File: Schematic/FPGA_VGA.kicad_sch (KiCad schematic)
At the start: 5 parts, among them U101 Upduino_3.0, Y101 25.175 MHz 7050 3.3V

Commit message: change host bus signal names to match logic
This was a bit of a tedious change, but I think it's
worthwhile to make it more obvious how the logic
and schematic relate to each other.
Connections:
- net HostA0 renamed HostBusAddr0
- net HostA1 renamed HostBusAddr1
- net HostA10 renamed HostBusAddr10
- net HostA2 renamed HostBusAddr2
- net HostA3 renamed HostBusAddr3
- net HostA4 renamed HostBusAddr4
- net HostA5 renamed HostBusAddr5
- net HostA6 renamed HostBusAddr6
- net HostA7 renamed HostBusAddr7
- net HostA8 renamed HostBusAddr8
- net HostA9 renamed HostBusAddr9
- net HostD0 renamed HostBusData0
- net HostD1 renamed HostBusData1
- net HostD2 renamed HostBusData2
- net HostD3 renamed HostBusData3
- net HostD4 renamed HostBusData4
- net HostD5 renamed HostBusData5
- net HostD6 renamed HostBusData6
- net HostD7 renamed HostBusData7
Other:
- sheet HostInterface ports: added HostBusAddr0, HostBusAddr1, HostBusAddr10, HostBusAddr2, HostBusAddr3, HostBusAddr4, HostBusAddr5, HostBusAddr6, HostBusAddr7, HostBusAddr8, HostBusAddr9, HostBusData0, HostBusData1, HostBusData2, HostBusData3, HostBusData4, HostBusData5, HostBusData6, HostBusData7; removed HostA0, HostA1, HostA10, HostA2, HostA3, HostA4, HostA5, HostA6, HostA7, HostA8, HostA9, HostD0, HostD1, HostD2, HostD3, HostD4, HostD5, HostD6, HostD7

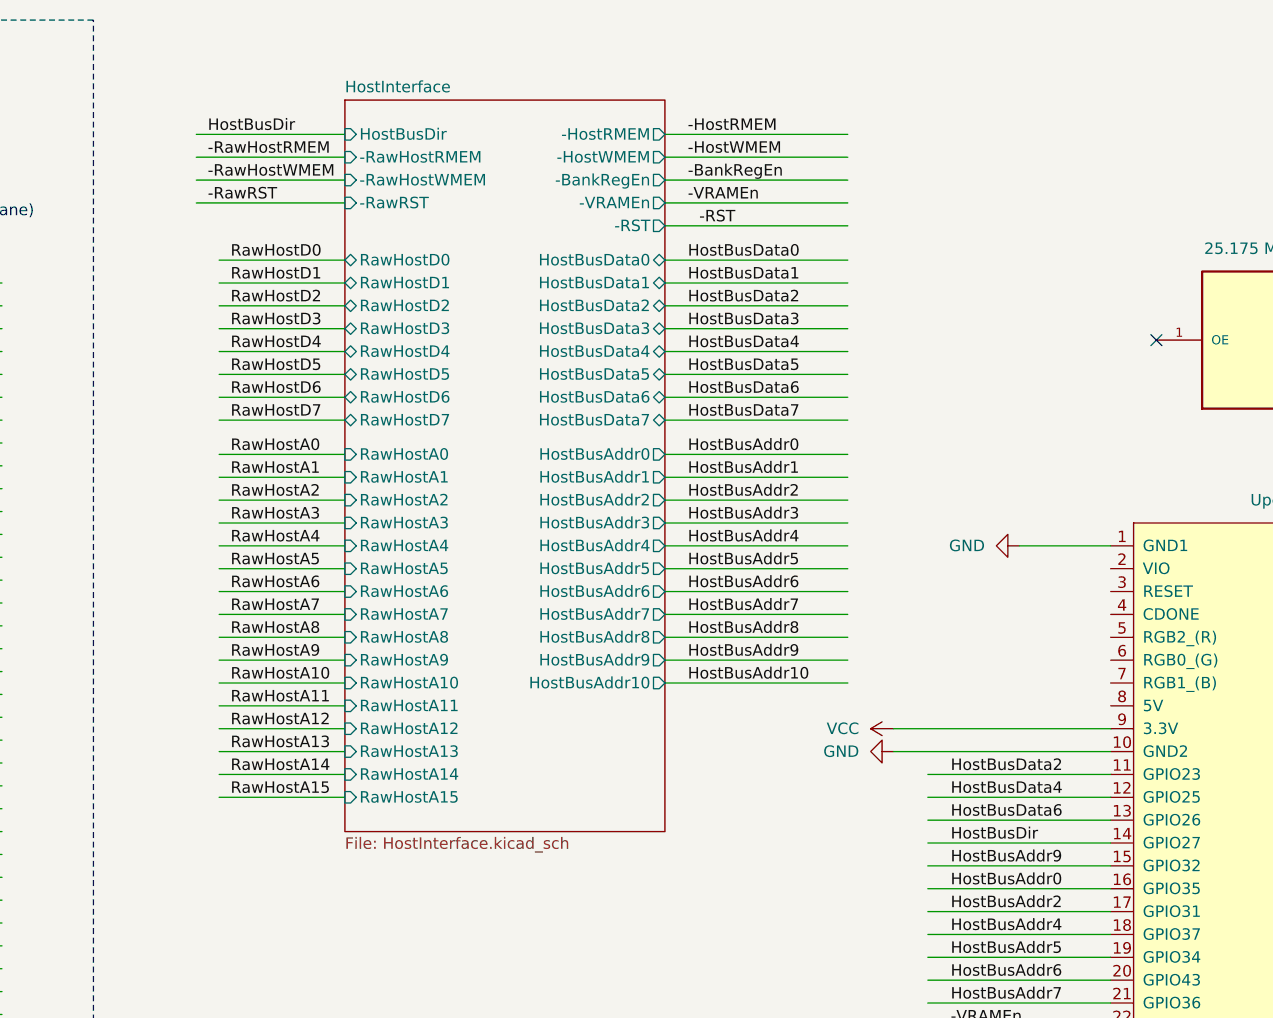
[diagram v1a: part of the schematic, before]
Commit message: connect FPGA 5V pin to host +5V
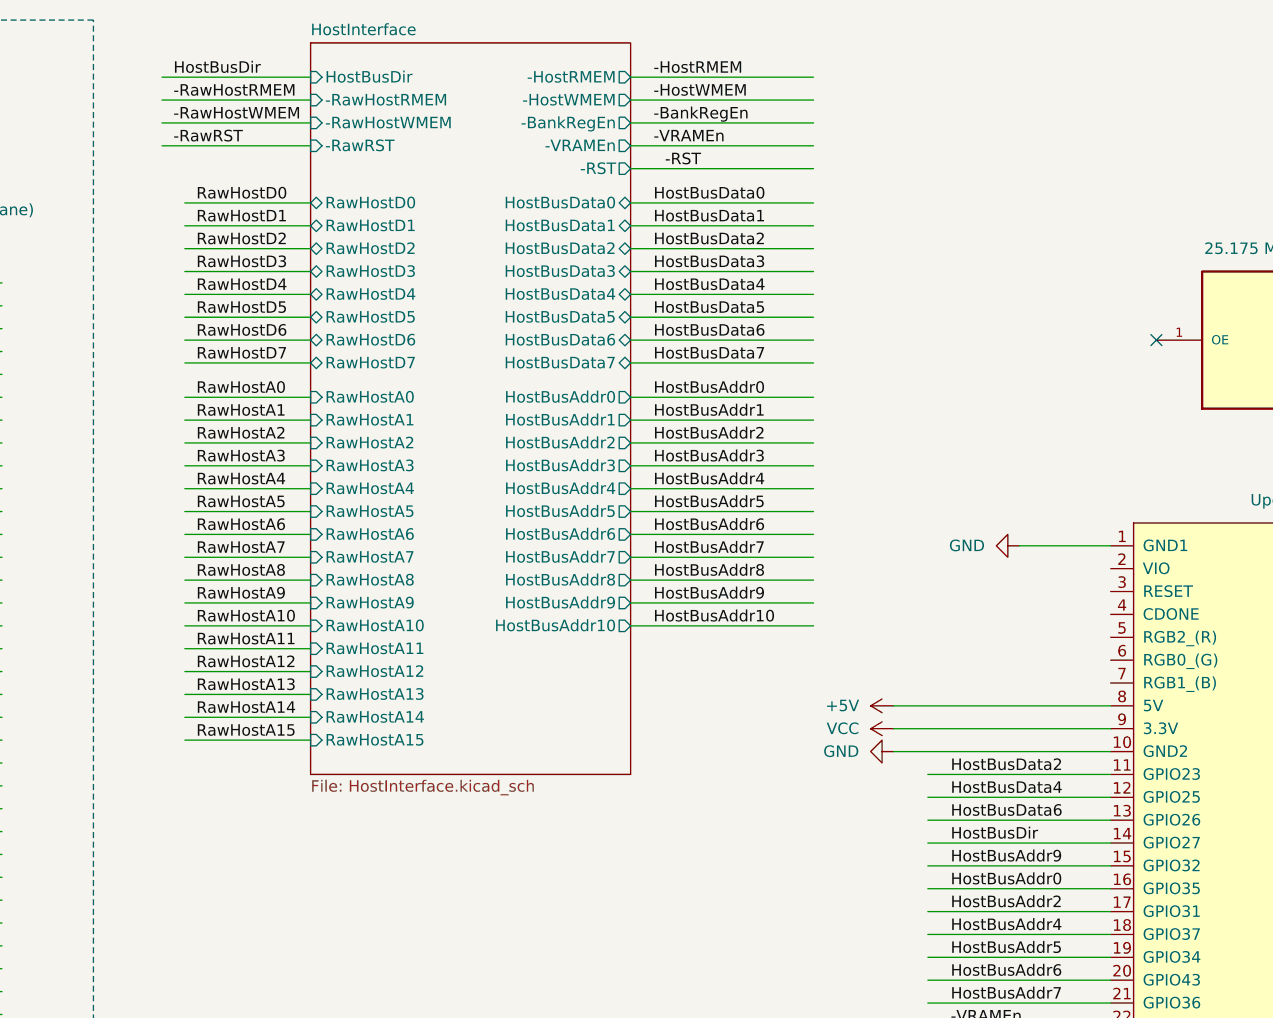
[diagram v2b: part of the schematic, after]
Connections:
- net +5V: now also U101.8 (5V)

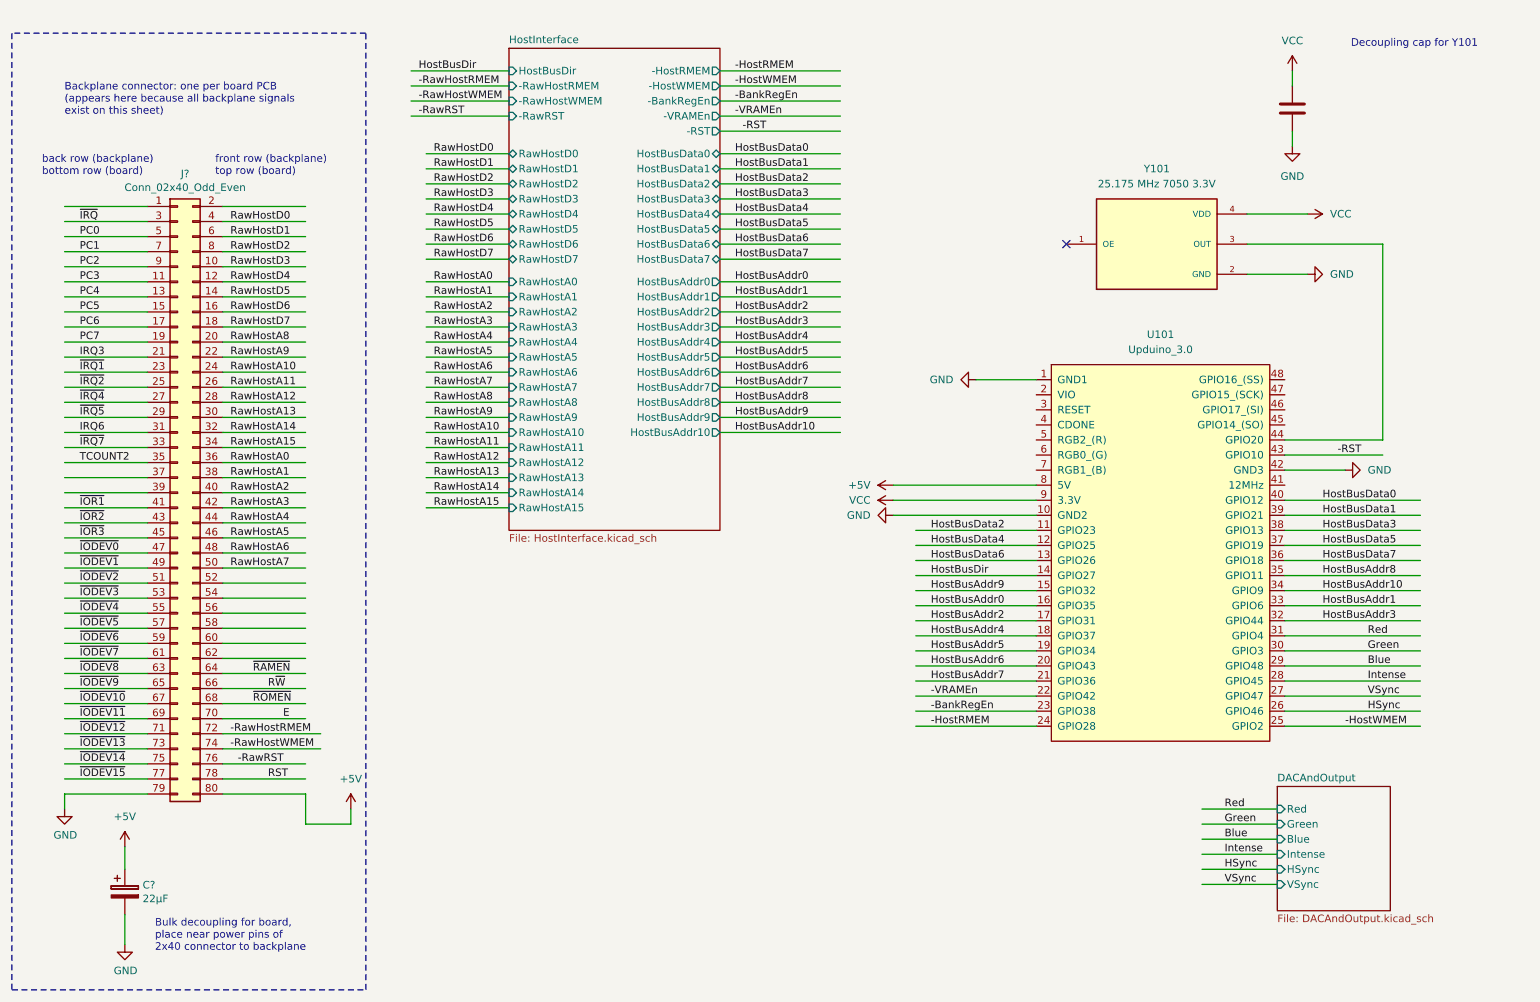
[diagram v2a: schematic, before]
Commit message: redesigning host interface
I think we will be able to do bidirectional I/O on
external pins, in order to communicate with the host
data bus.

Eliminating the bank register as part of the actual
display controller. Eventually I want the VRAM to be
mapped into a single 8 KB window. If the host system
needs a bank register, it can be external to the
display controller.
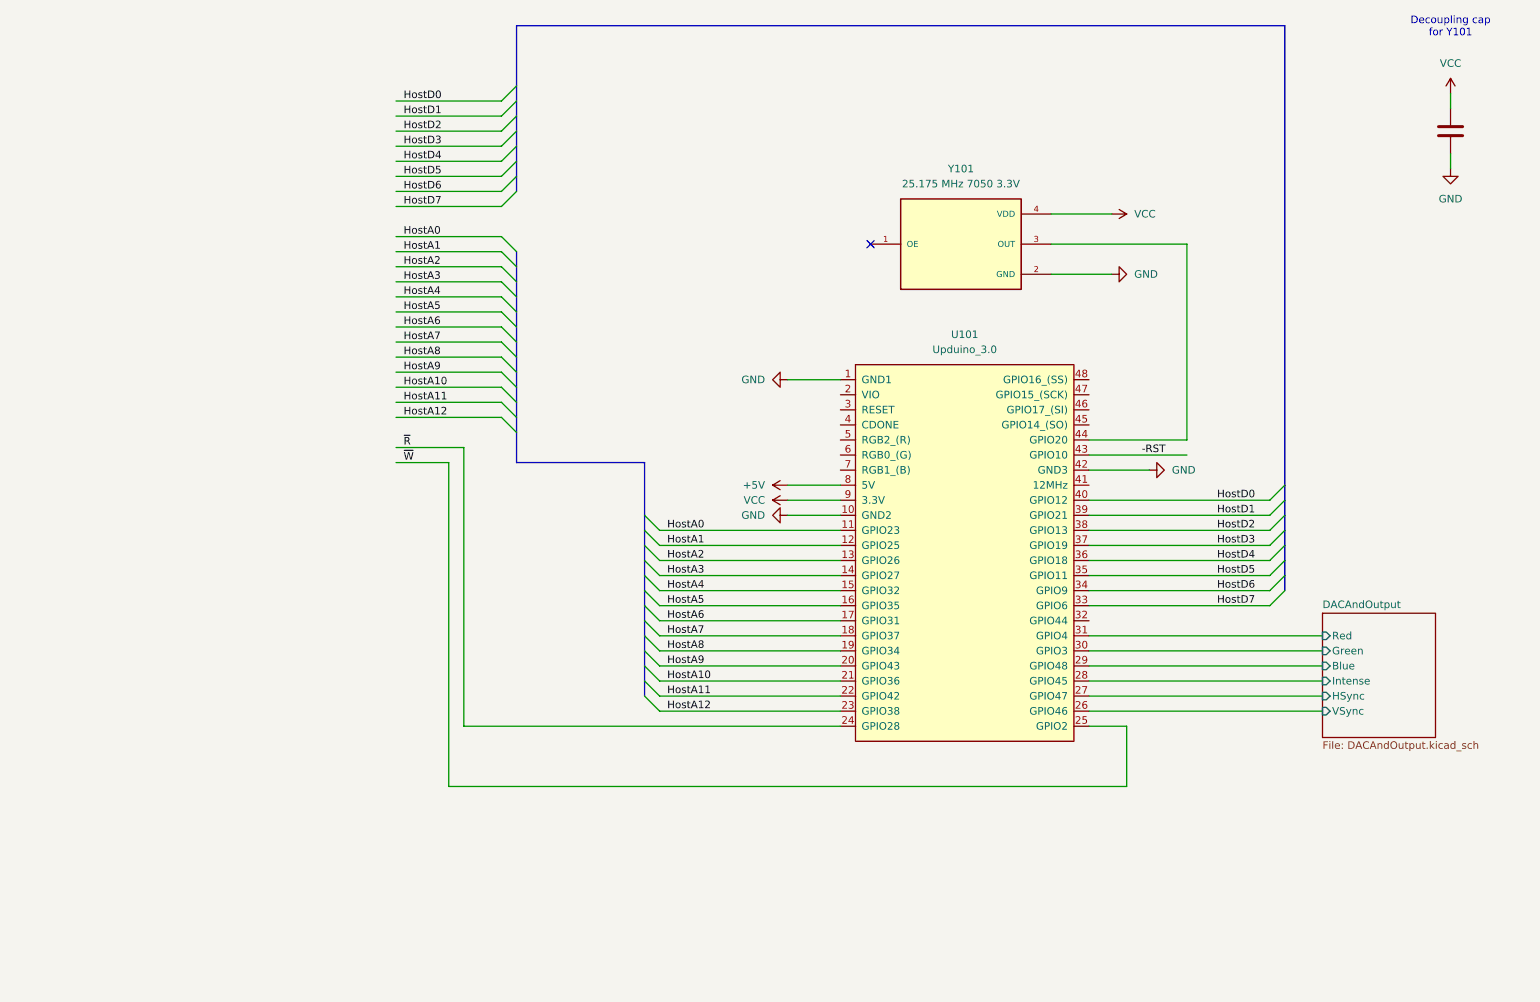
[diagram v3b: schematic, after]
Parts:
- removed C?: 22μF, Capacitor_THT:CP_Radial_D6.3mm_P2.50mm, symbol device:CP
- removed J?: Conn_02x40_Odd_Even, Connector_PinHeader_2.54mm:PinHeader_2x40_P2.54mm_Vertical, symbol Connector_Generic:Conn_02x40_Odd_Even
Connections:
- net -BankRegEn renamed HostA12
- net -HostRMEM renamed ~{R}
- net -HostWMEM renamed ~{W}
- net -VRAMEn renamed HostA11
- net Blue renamed DACAndOutput/Blue
- net Green renamed DACAndOutput/Green
- net HSync renamed DACAndOutput/VSync
- net HostBusAddr0 renamed HostA5
- net HostBusAddr1 renamed HostD7
- net HostBusAddr10 renamed HostD6
- net HostBusAddr2 renamed HostA6
- net HostBusAddr3: no longer names the net of U101.32 (GPIO44)
- net HostBusAddr4 renamed HostA7
- net HostBusAddr5 renamed HostA8
- net HostBusAddr6 renamed HostA9
- net HostBusAddr7 renamed HostA10
- net HostBusAddr8 renamed HostD5
- net HostBusAddr9 renamed HostA4
- net HostBusData0 renamed HostD0
- net HostBusData1 renamed HostD1
- net HostBusData2 renamed HostA0
- net HostBusData3 renamed HostD2
- net HostBusData4 renamed HostA1
- net HostBusData5 renamed HostD3
- net HostBusData6 renamed HostA2
- net HostBusData7 renamed HostD4
- net HostBusDir renamed HostA3
- net Intense renamed DACAndOutput/Intense
- net Red renamed DACAndOutput/Red
- net VSync renamed DACAndOutput/HSync
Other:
- removed sheet HostInterface
- note removed: "Backplane connector: one per board PCB (appears here because all backplane signals exist on this sheet)"
- note removed: "Bulk decoupling for board, place near power pins of 2x40 connector to backplane"
- note removed: "back row (backplane) bottom row (board)"
- note removed: "front row (backplane) top row (board)"
- moved on the sheet: U101, Y101
